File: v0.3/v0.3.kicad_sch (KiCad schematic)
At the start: 0 parts

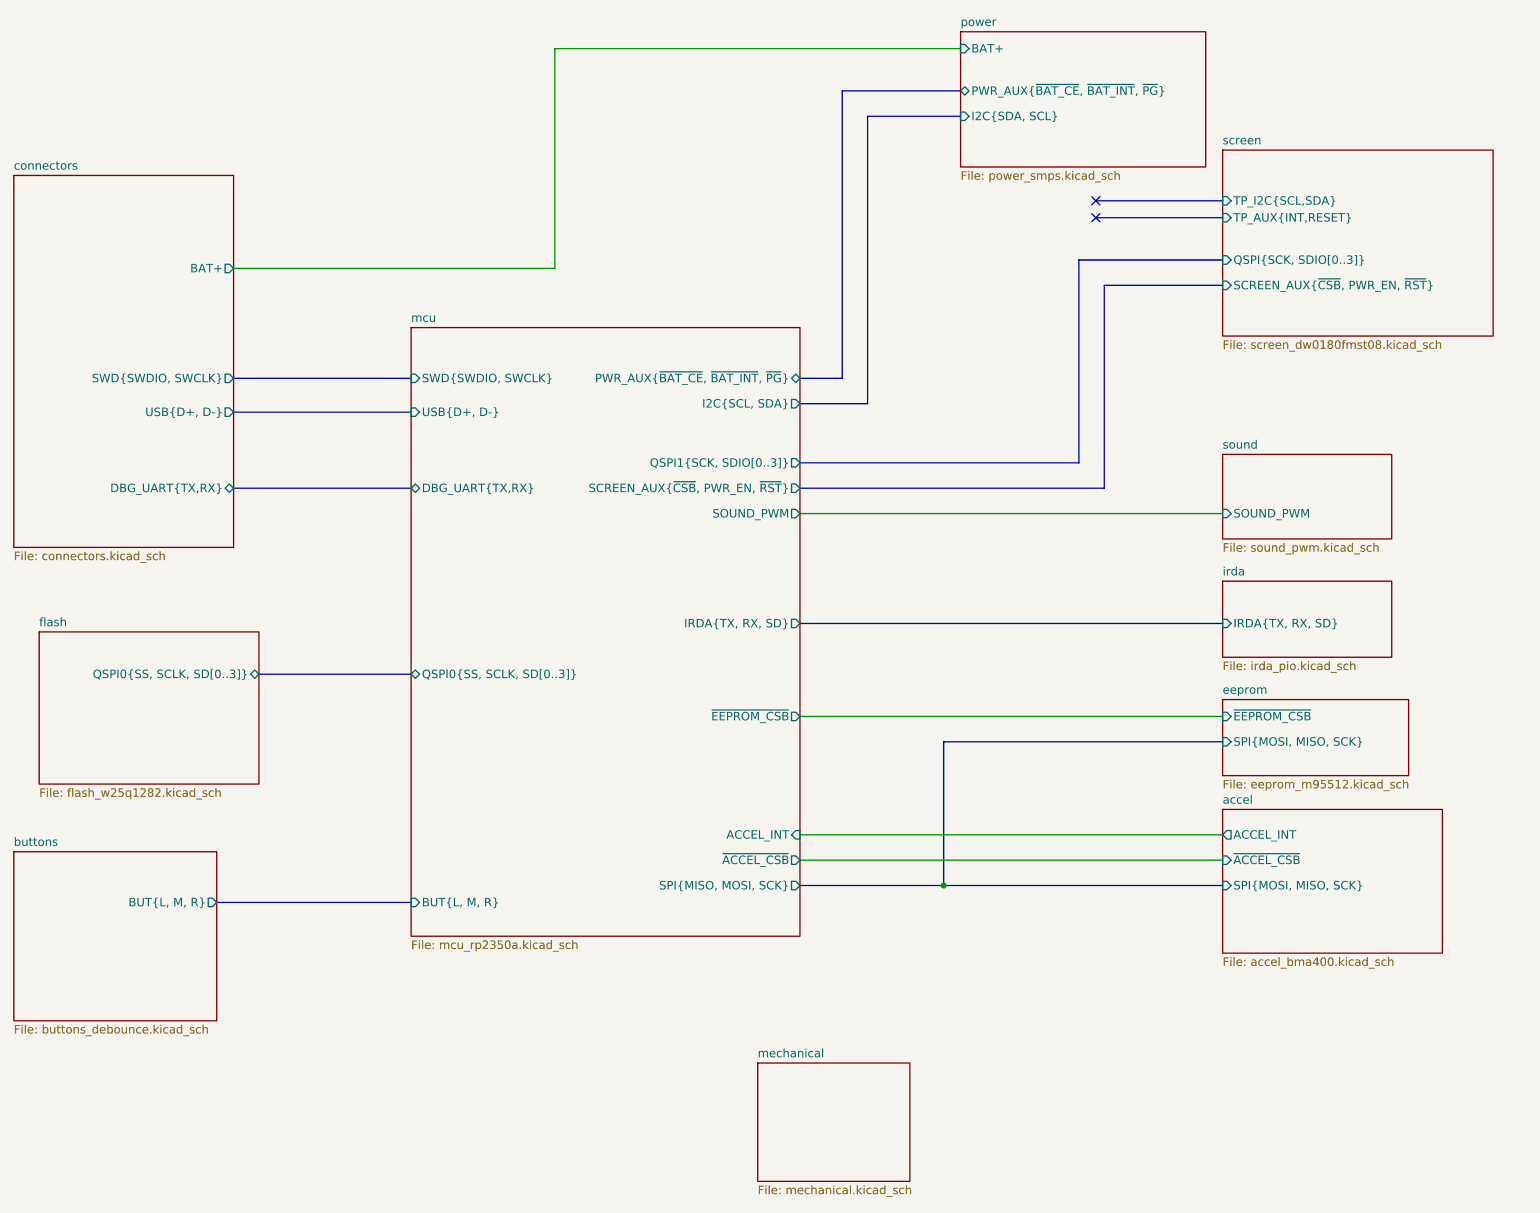
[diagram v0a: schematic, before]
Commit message: v0.3: move pmic to right side of board
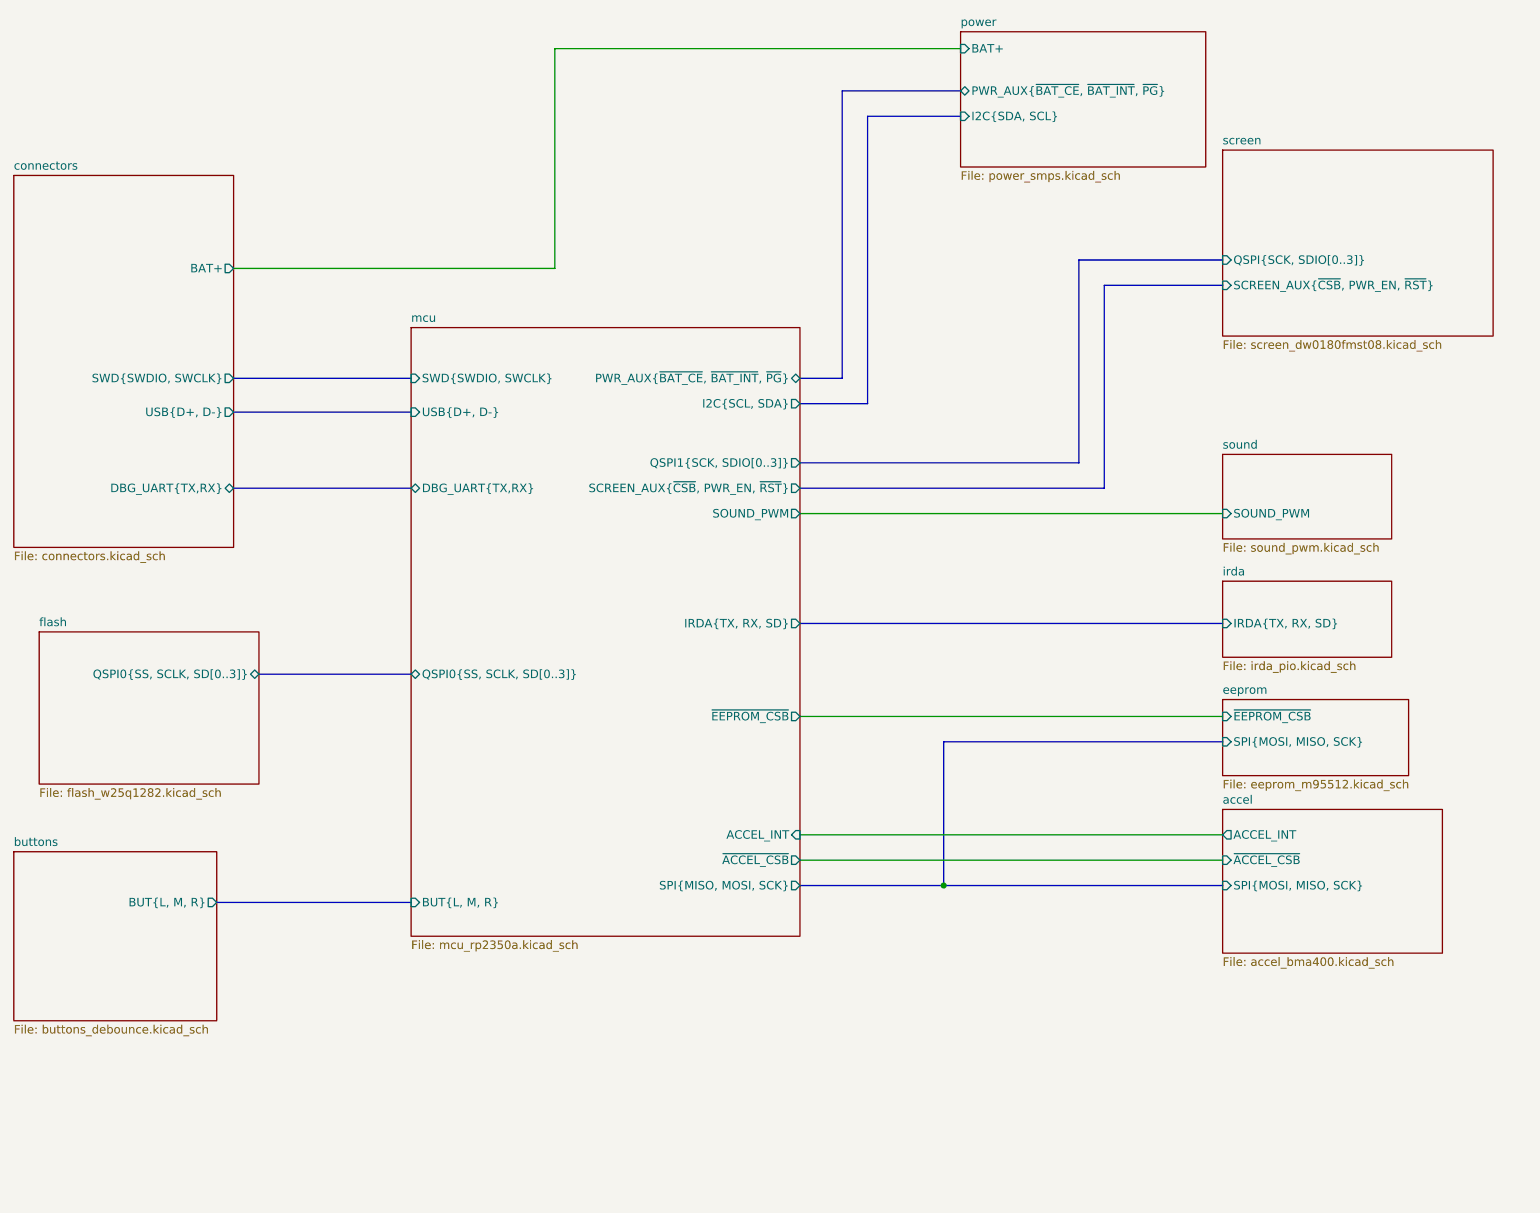
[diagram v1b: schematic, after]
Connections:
- no-connect marks 2 -> 0
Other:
- removed sheet mechanical
- sheet screen ports: added none; removed TP_AUX{INT,RESET}, TP_I2C{SCL,SDA}
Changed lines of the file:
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@@
 		(color 0 0 0 0)
 	)
-	(no_connect
-		(at 191.77 46.99)
-	)
-	(no_connect
-		(at 191.77 44.45)
-	)
 	(bus
 		(pts
@@
 		)
 	)
-	(bus
-		(pts
-			(xy 191.77 46.99) (xy 210.82 46.99)
-		)
-		(stroke
-			(width 0)
-			(type default)
-		)
-	)
 	(wire
 		(pts
@@
 		(pts
 			(xy 62.23 87.63) (xy 88.9 87.63)
-		)
-		(stroke
-			(width 0)
-			(type default)
-		)
-	)
-	(bus
-		(pts
-			(xy 191.77 44.45) (xy 210.82 44.45)
 		)
 		(stroke
@@
 	)
 	(sheet
-		(at 140.97 173.99)
-		(size 22.86 17.78)
-		(exclude_from_sim no)
-		(in_bom yes)
-		(on_board yes)
-		(dnp no)
-		(fields_autoplaced yes)
-		(stroke
-			(width 0.1524)
-			(type solid)
-		)
-		(fill
-			(color 0 0 0 0.0000)
-		)
-		(property "Sheetname" "mechanical"
-			(at 140.97 173.2784 0)
-			(effects
-				(font
-					(size 1.27 1.27)
-				)
-				(justify left bottom)
-			)
-		)
-		(property "Sheetfile" "mechanical.kicad_sch"
-			(at 140.97 192.3546 0)
-			(effects
-				(font
-					(size 1.27 1.27)
-				)
-				(justify left top)
-			)
-		)
-		(instances
-			(project "v0.3"
-				(path "/5cbb45d4-7f83-48dd-a53b-5c75c7d1d827"
-					(page "10")
-				)
-			)
-		)
-	)
-	(sheet
 		(at 210.82 119.38)
 		(size 27.94 11.43)
@@
 			(effects
 				(font
-					(size 1.27 1.27)
-				)
-				(justify left)
-			)
-		)
-		(pin "TP_I2C{SCL,SDA}" input
-			(at 210.82 44.45 180)
-			(effects
-				(font
-					(size 1.27 1.27)
-				)
-				(justify left)
-			)
-		)
-		(pin "TP_AUX{INT,RESET}" input
-			(at 210.82 46.99 180)
-			(effects
-				(font
